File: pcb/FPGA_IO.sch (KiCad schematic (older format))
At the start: 8 parts, among them J2 JSHORTNORMAL, J3 JSHORTNORMAL, U4 iCE40-HX8K-CT256, U7 OSC

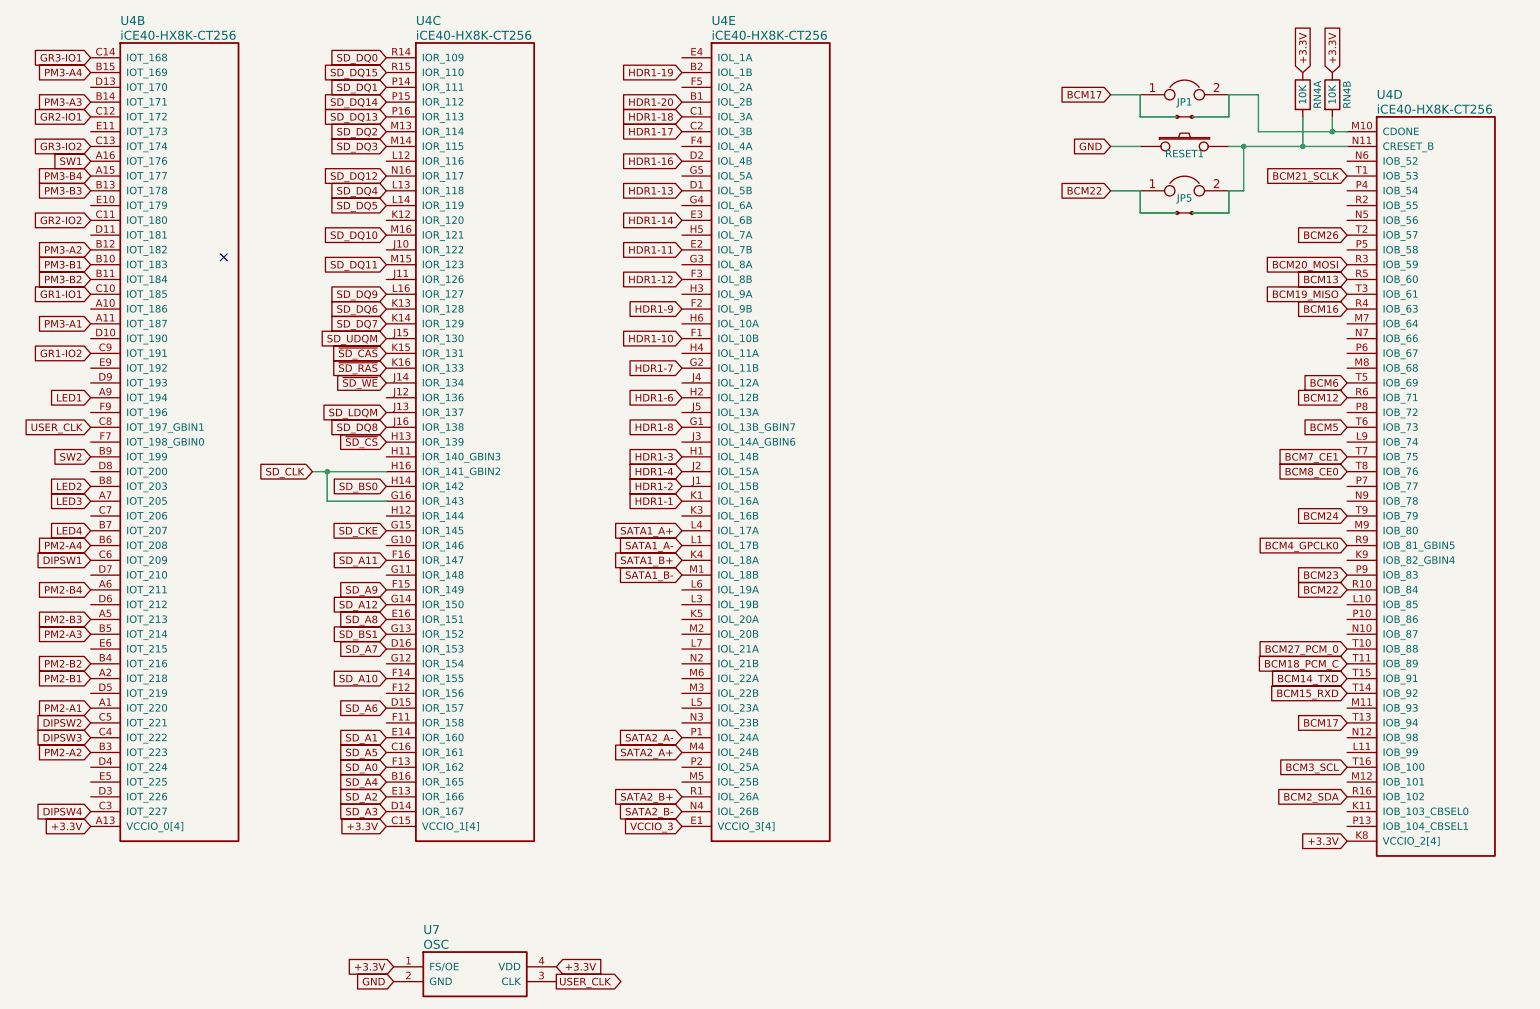
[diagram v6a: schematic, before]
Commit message: Spreading wires, arranging components.
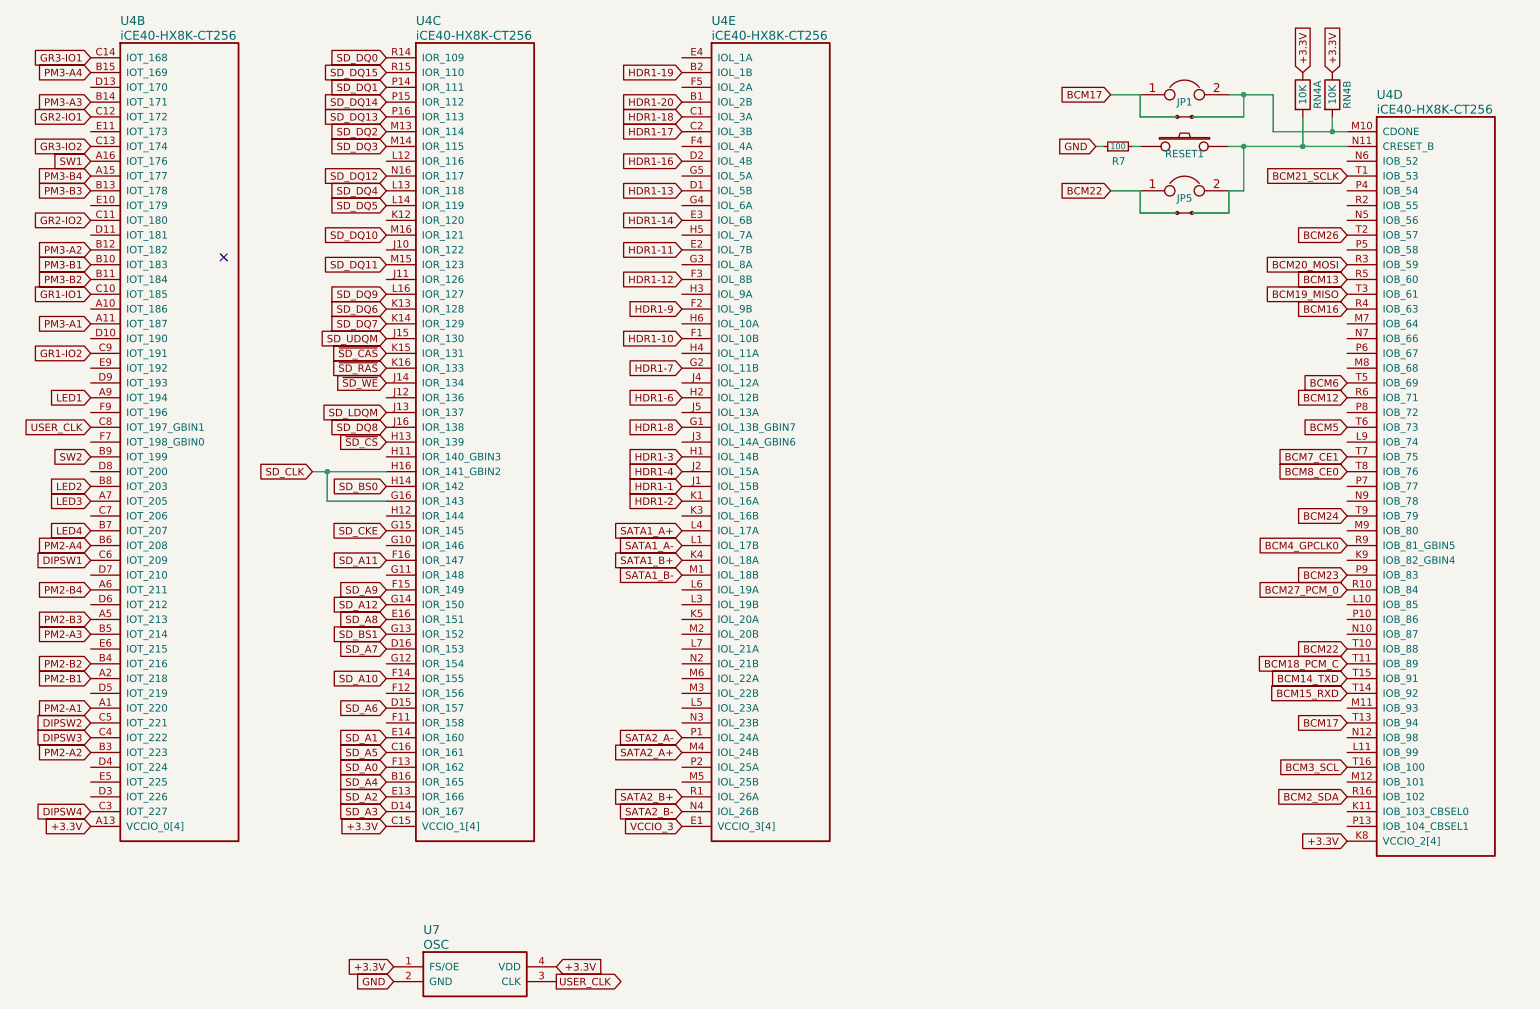
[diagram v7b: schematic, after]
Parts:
- added R7: 100, Resistors_SMD:R_0603, symbol R_Small
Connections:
- net BCM22: now also U4.T10 (IOB_88); no longer U4.R10 (IOB_84)
- net BCM27_PCM_0: now also U4.R10 (IOB_84); no longer U4.T10 (IOB_88)
- net GND: now also R7.1; no longer RESET1.1
- net HDR1-1: now also U4.J1 (IOL_15B); no longer U4.K1 (IOL_16A)
- net HDR1-2: now also U4.K1 (IOL_16A); no longer U4.J1 (IOL_15B)
- new net: R7.2, RESET1.1
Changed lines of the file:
@@
 1E 25 49 2A DA F6 C4 5C B7 0C C3 B9 A4 0A 98 09 FC 0D B0 92 CD 57 CD 1F 06 4E 04 26 A7 75 27 49
 52 39 26 13 73 DE C3 6C BE 70 B5 12 F8 16 86 73 8D C3 FF 03 63 F8 EE 2E BE 9A 04 B1 00 00 00 00
-49 45 4E 44 AE 42 60 82 E6
+49 45 4E 44 AE 42 60 82 71
 EndData
 $EndBitmap
@@
 	0    -1   -1   0
 $EndComp
-Wire Wire Line
-	9300 1400 9900 1400
-Wire Wire Line
-	9800 1400 9800 1300
-Connection ~ 9800 1400
 Text GLabel 9600 1000 1    50   Input ~ 0
 +3.3V
@@
 Text GLabel 9900 3400 0    50   Input ~ 0
 BCM5
+Text GLabel 9900 4900 0    50   Input ~ 0
+BCM22
 Text GLabel 9900 4500 0    50   Input ~ 0
-BCM22
-Text GLabel 9900 4900 0    50   Input ~ 0
 BCM27_PCM_0
 Text GLabel 9900 5400 0    50   Input ~ 0
@@
 	1    0    0    -1
 $EndComp
-Text GLabel 8300 1500 0    50   Input ~ 0
+Text GLabel 8200 1500 0    50   Input ~ 0
 GND
 $Comp
@@
 	1    0    0    -1
 $EndComp
-Wire Wire Line
-	9300 1400 9300 1150
-Wire Wire Line
-	9300 1150 9100 1150
 Text GLabel 8300 1150 0    50   Input ~ 0
 BCM17
@@
 Text GLabel 5400 6000 0    50   Input ~ 0
 SATA2_B-
-Text GLabel 5400 3900 0    50   Input ~ 0
+Text GLabel 5400 3800 0    50   Input ~ 0
 HDR1-1
 Text GLabel 5400 3700 0    50   Input ~ 0
@@
 Text GLabel 5400 3000 0    50   Input ~ 0
 HDR1-7
-Text GLabel 5400 3800 0    50   Input ~ 0
+Text GLabel 5400 3900 0    50   Input ~ 0
 HDR1-2
 Text GLabel 5400 3600 0    50   Input ~ 0
@@
 	8500 1150 8300 1150
 Wire Wire Line
-	8500 1500 8300 1500
-Wire Wire Line
 	8500 1800 8300 1800
-Wire Wire Line
-	9100 1150 9100 1300
-Wire Wire Line
-	9100 1300 8850 1300
 Wire Wire Line
 	8750 1300 8500 1300
@@
 Text GLabel 1400 1500 0    50   Input ~ 0
 GR3-IO2
+Wire Wire Line
+	8850 1300 9200 1300
+Wire Wire Line
+	9200 1300 9200 1150
+Wire Wire Line
+	9100 1150 9400 1150
+Wire Wire Line
+	9400 1150 9400 1400
+Wire Wire Line
+	9400 1400 9900 1400
+Connection ~ 9200 1150
+Wire Wire Line
+	9800 1300 9800 1400
+Connection ~ 9800 1400
+$Comp
+L R_Small R7
+U 1 1 55FA4B25
+P 8350 1500
+F 0 "R7" V 8250 1450 50  0000 L CNN
+F 1 "100" V 8350 1500 40  0000 C CNN
+F 2 "Resistors_SMD:R_0603" H 8350 1500 60  0001 C CNN
+F 3 "" H 8350 1500 60  0000 C CNN
+	1    8350 1500
+	0    -1   -1   0
+$EndComp
+Wire Wire Line
+	8200 1500 8250 1500
+Wire Wire Line
+	8450 1500 8500 1500
 $EndSCHEMATC

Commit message: All layout done except for placing test points and arranging silkscreen.
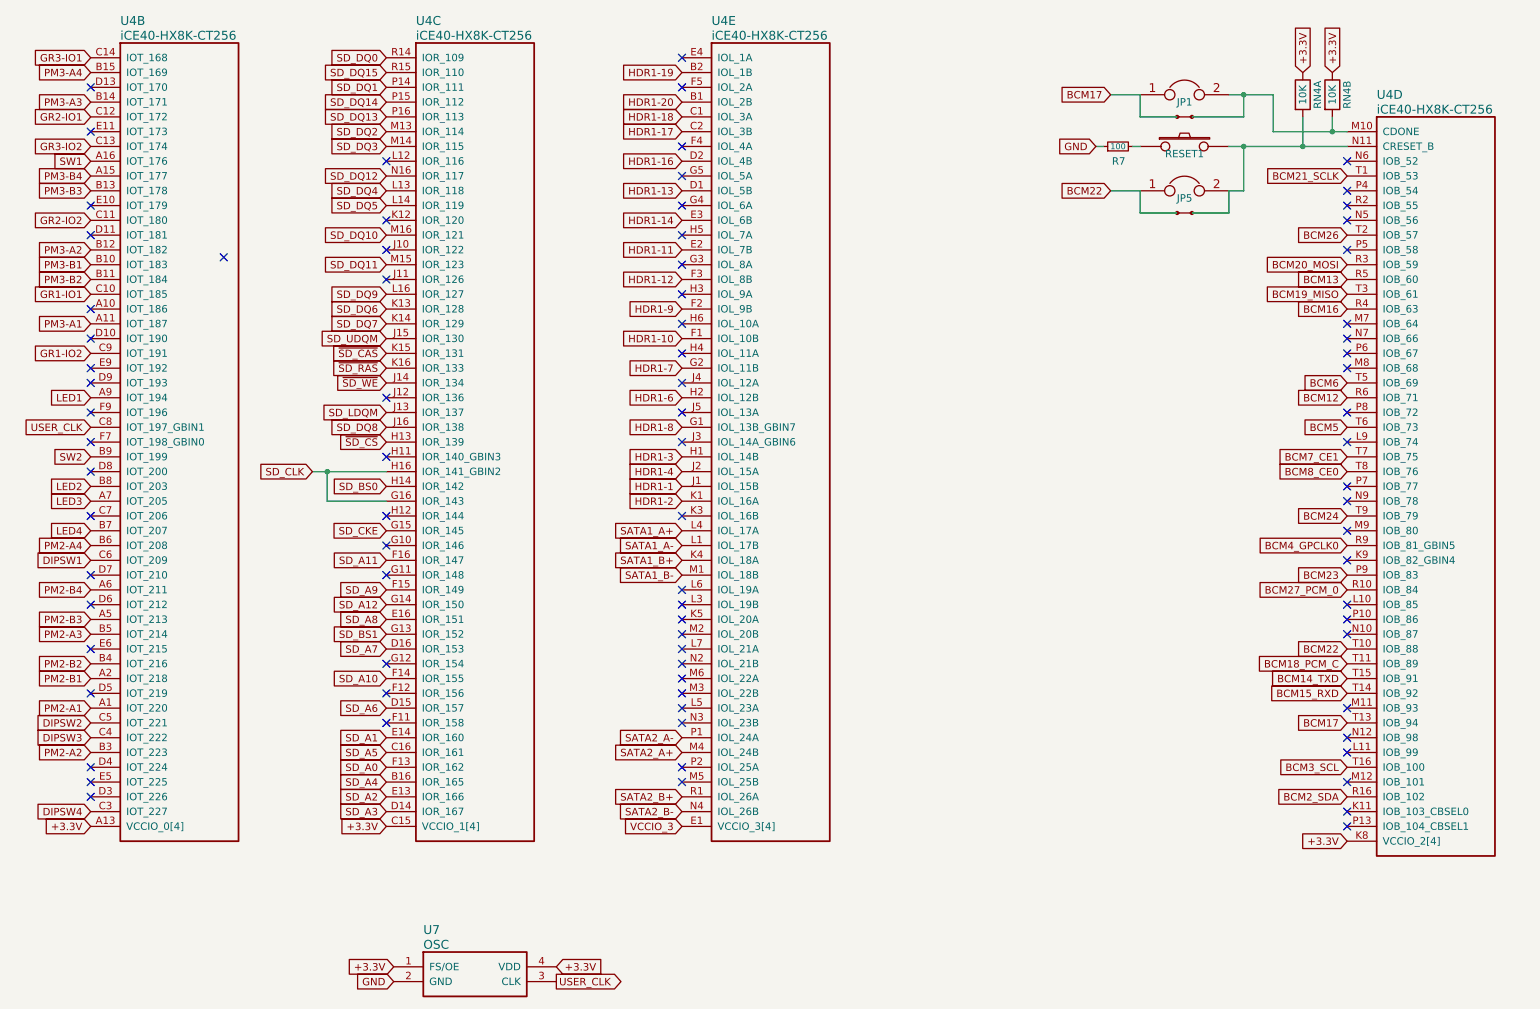
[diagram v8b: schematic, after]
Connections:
- no-connect marks 1 -> 82
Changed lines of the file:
@@
 1E 25 49 2A DA F6 C4 5C B7 0C C3 B9 A4 0A 98 09 FC 0D B0 92 CD 57 CD 1F 06 4E 04 26 A7 75 27 49
 52 39 26 13 73 DE C3 6C BE 70 B5 12 F8 16 86 73 8D C3 FF 03 63 F8 EE 2E BE 9A 04 B1 00 00 00 00
-49 45 4E 44 AE 42 60 82 71
+49 45 4E 44 AE 42 60 82 73
 EndData
 $EndBitmap
@@
 Wire Wire Line
 	8450 1500 8500 1500
+NoConn ~ 5400 5800
+NoConn ~ 5400 5700
+NoConn ~ 5400 5400
+NoConn ~ 5400 5300
+NoConn ~ 5400 5200
+NoConn ~ 5400 5100
+NoConn ~ 5400 5000
+NoConn ~ 5400 4900
+NoConn ~ 5400 4800
+NoConn ~ 5400 4700
+NoConn ~ 5400 4600
+NoConn ~ 5400 4500
+NoConn ~ 3400 5400
+NoConn ~ 3400 5200
+NoConn ~ 3400 5000
+NoConn ~ 3400 4400
+NoConn ~ 3400 4200
+NoConn ~ 1400 5900
+NoConn ~ 1400 5800
+NoConn ~ 1400 5700
+NoConn ~ 1400 5200
+NoConn ~ 1400 4900
+NoConn ~ 1400 4600
+NoConn ~ 1400 4400
+NoConn ~ 1400 4000
+NoConn ~ 1400 3700
+NoConn ~ 1400 3500
+NoConn ~ 1400 3300
+NoConn ~ 1400 3100
+NoConn ~ 1400 3000
+NoConn ~ 1400 2800
+NoConn ~ 1400 2600
+NoConn ~ 1400 2100
+NoConn ~ 1400 1900
+NoConn ~ 1400 1400
+NoConn ~ 1400 1100
+NoConn ~ 3400 1600
+NoConn ~ 3400 2000
+NoConn ~ 3400 2200
+NoConn ~ 3400 2400
+NoConn ~ 3400 3200
+NoConn ~ 3400 3600
+NoConn ~ 3400 4000
+NoConn ~ 5400 900
+NoConn ~ 5400 1100
+NoConn ~ 5400 1500
+NoConn ~ 5400 1700
+NoConn ~ 5400 1900
+NoConn ~ 5400 2100
+NoConn ~ 5400 2300
+NoConn ~ 5400 2500
+NoConn ~ 5400 2700
+NoConn ~ 5400 2900
+NoConn ~ 5400 3100
+NoConn ~ 5400 3300
+NoConn ~ 5400 3500
+NoConn ~ 5400 4000
+NoConn ~ 9900 1600
+NoConn ~ 9900 1800
+NoConn ~ 9900 1900
+NoConn ~ 9900 2000
+NoConn ~ 9900 2200
+NoConn ~ 9900 2700
+NoConn ~ 9900 2800
+NoConn ~ 9900 2900
+NoConn ~ 9900 3000
+NoConn ~ 9900 3300
+NoConn ~ 9900 3500
+NoConn ~ 9900 3800
+NoConn ~ 9900 3900
+NoConn ~ 9900 4100
+NoConn ~ 9900 4300
+NoConn ~ 9900 4600
+NoConn ~ 9900 4700
+NoConn ~ 9900 4800
+NoConn ~ 9900 5300
+NoConn ~ 9900 5500
+NoConn ~ 9900 5600
+NoConn ~ 9900 5800
+NoConn ~ 9900 6000
+NoConn ~ 9900 6100
 $EndSCHEMATC
